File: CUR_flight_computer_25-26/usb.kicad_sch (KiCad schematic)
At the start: 4 parts, among them J12 UJ20-C-H-G-SMT-5-P16-TR, U14 USBLC6-2SC6

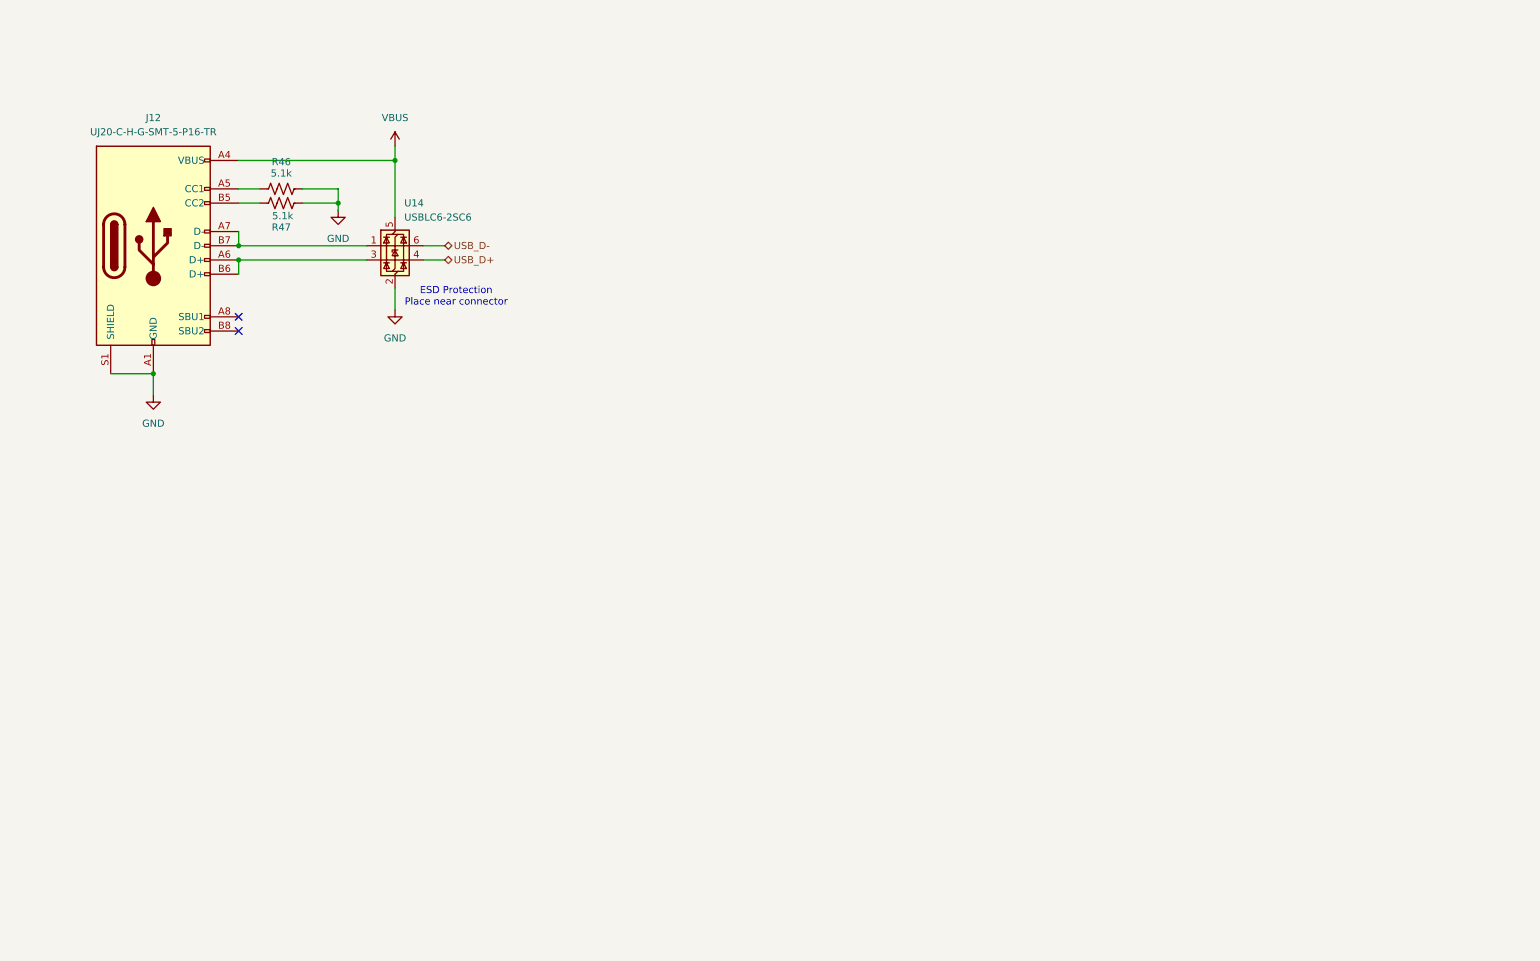
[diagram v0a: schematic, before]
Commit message: Cleaned up schematic
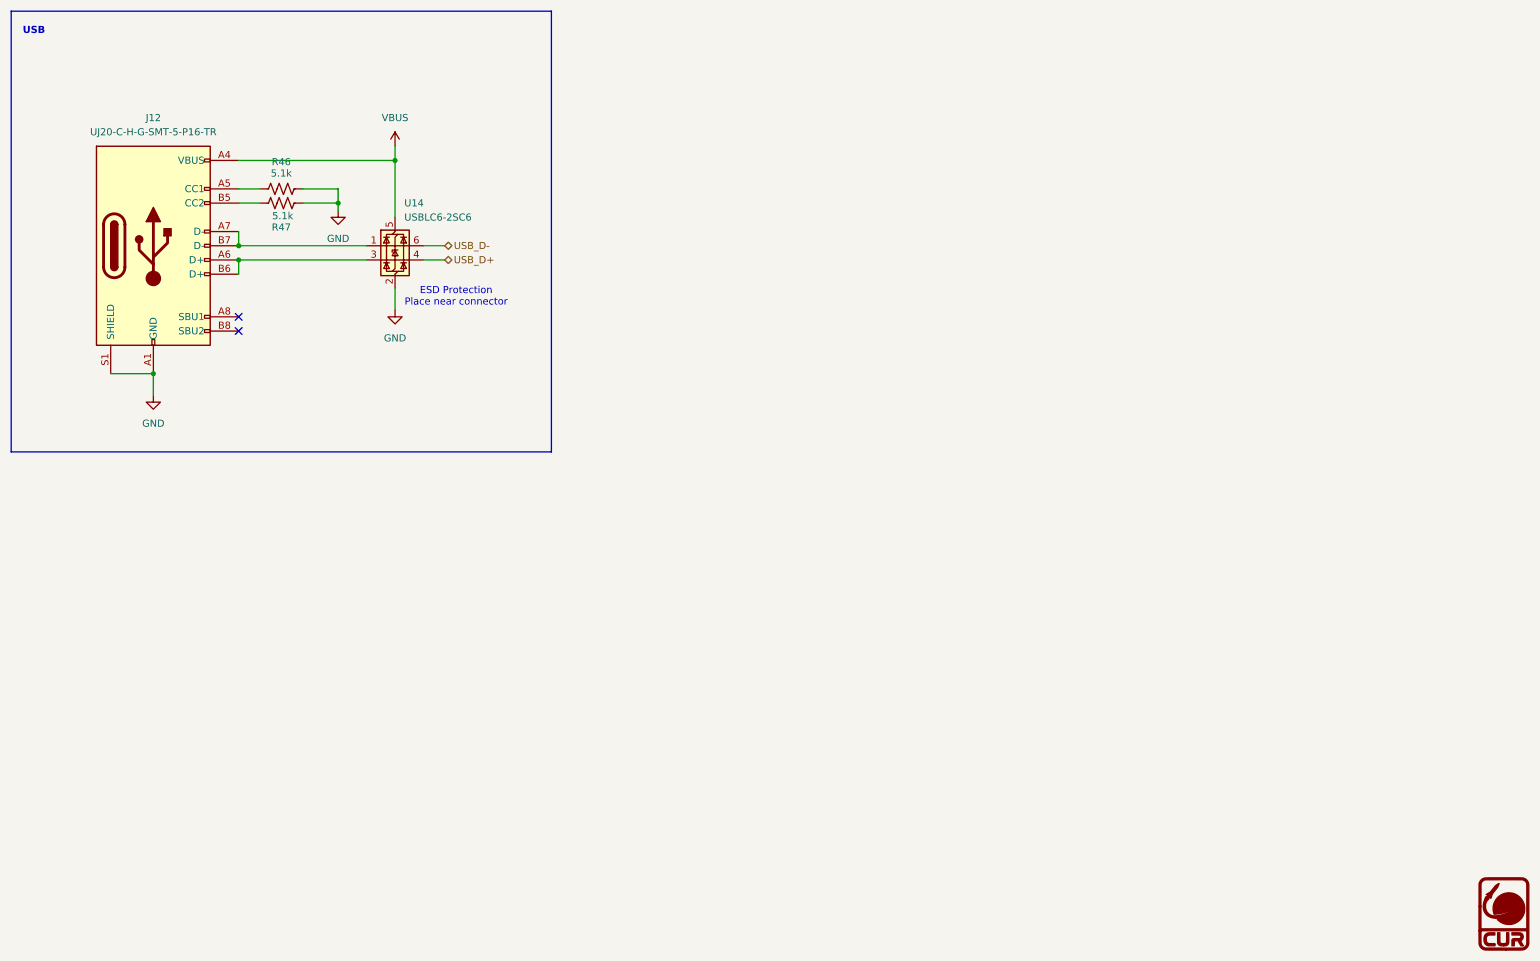
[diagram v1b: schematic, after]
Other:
- note added: "USB"
- company: (none) -> Clarkson University Rocketry
- title: (none) -> Flight Computer
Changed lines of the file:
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@@
 	(generator_version "9.0")
 	(paper "A4")
+	(title_block
+		(title "Flight Computer")
+		(date "2026-03-18")
+		(company "Clarkson University Rocketry")
+	)
+	(rectangle
+		(start 12.7 12.7)
+		(end 109.22 91.44)
+		(stroke
+			(width 0)
+			(type default)
+		)
+		(fill
+			(type none)
+		)
+	)
 	(text "ESD Protection\nPlace near connector"
 		(exclude_from_sim no)
@@
 			(font
 				(size 1.27 1.27)
+			)
+		)
+	)
+	(text "USB"
+		(exclude_from_sim no)
+		(at 16.764 16.256 0)
+		(effects
+			(font
+				(size 1.27 1.27)
+				(thickness 0.254)
+				(bold yes)
 			)
 		)
@@
 					(unit 1)
 				)
+			)
+		)
+	)
+	(symbol
+		(lib_id "CUR_Logo:LOGO")
+		(at 279.4 173.99 0)
+		(unit 1)
+		(exclude_from_sim no)
+		(in_bom yes)
+		(on_board yes)
+		(dnp no)
+		(fields_autoplaced yes)
+		(property "Reference" "#G10"
+			(at 279.4 167.002 0)
+			(effects
+				(font
+					(size 1.27 1.27)
+				)
+				(hide yes)
+			)
+		)
+		(property "Value" "LOGO"
+			(at 279.4 180.978 0)
+			(effects
+				(font
+					(size 1.27 1.27)
+				)
+				(hide yes)
+			)
+		)
+		(property "Footprint" ""
+			(at 279.4 173.99 0)
+			(effects
+				(font
+					(size 1.27 1.27)
+				)
+				(hide yes)
+			)
+		)
+		(property "Datasheet" ""
+			(at 279.4 173.99 0)
+			(effects
+				(font
+					(size 1.27 1.27)
+				)
+				(hide yes)
+			)
+		)
+		(property "Description" ""
+			(at 279.4 173.99 0)
+			(effects
+				(font
+					(size 1.27 1.27)
+				)
+				(hide yes)
+			)
+		)
+		(instances
+			(project "CUR_flight_computer_25-26"
+				(path "/bf7761cc-1b32-4d86-809c-5f027005229b/cf63387d-37b0-4f5e-affd-1b765436078d"
+					(reference "#G10")
+					(unit 1)
+				)
